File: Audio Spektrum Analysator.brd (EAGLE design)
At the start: 144.8 x 98.7 mm, 157 parts, among them IC1 LM324N, IC10 LM3914N, IC11 LM3914N, IC12 LM3914N, IC13 LM3914N, IC2 LM324N, IC3 LM324N, IC4 LM3914N, IC5 LM3914N, IC6 LM3914N, IC7 LM3914N, IC8 LM3914N, IC9 LM3914N, J2 DCJ0202, M1 ELECTRET_MICROPHON-F6050AP

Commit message: moved names, added testpoints
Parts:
- added TP4, TP5: TPPAD1-20, testpad:P1-20
- moved TP3 46.9 mm to (108.0, 12.7)
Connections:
- net RHI: now also TP4.TP
- net RLO: now also TP5.TP
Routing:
- net RLO: track 149.6 -> 171.8 mm, vias 9 -> 11
- net RHI: track 163.9 -> 183.0 mm, vias 0 -> 1
- net VER: track 176.2 -> 172.2 mm

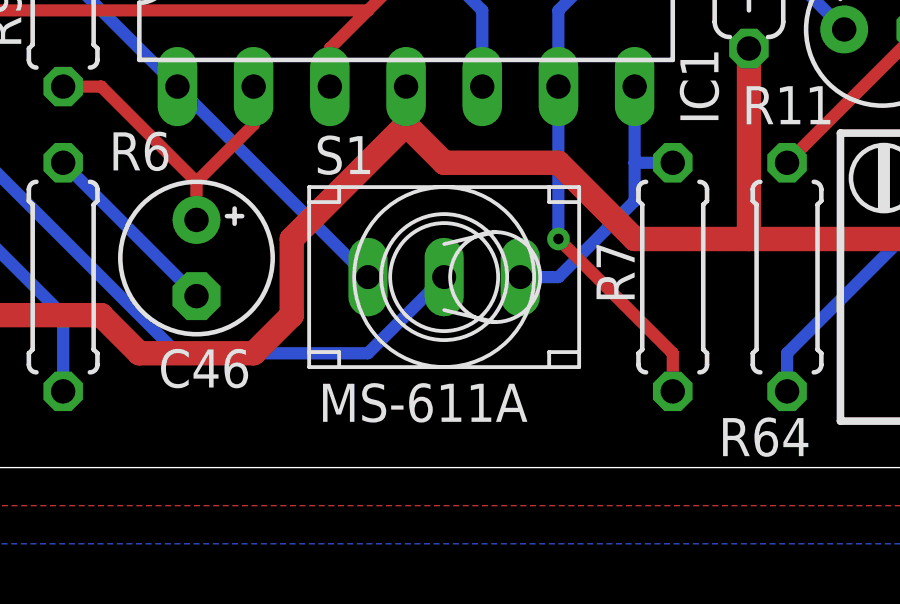
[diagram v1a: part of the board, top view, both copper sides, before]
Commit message: replaced s1
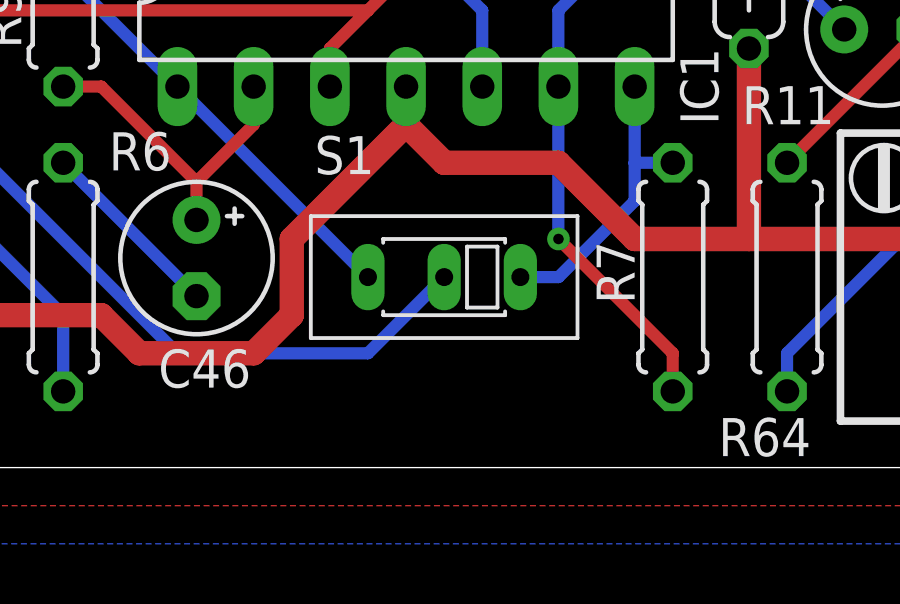
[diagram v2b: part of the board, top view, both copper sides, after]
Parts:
- S1: value MS-611A -> SPDT; device 1_Robo-Lib:MS-611A -> Jakobs_LBR:SPDT
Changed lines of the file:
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@@
 <layer number="44" name="Drills" color="7" fill="1" visible="yes" active="yes"/>
 <layer number="45" name="Holes" color="7" fill="1" visible="yes" active="yes"/>
-<layer number="46" name="Milling" color="3" fill="1" visible="no" active="yes"/>
+<layer number="46" name="Milling" color="3" fill="1" visible="yes" active="yes"/>
 <layer number="47" name="Measures" color="7" fill="1" visible="no" active="yes"/>
 <layer number="48" name="Document" color="7" fill="1" visible="no" active="yes"/>
@@
 <attribute name="VALUE" x="43.2562" y="68.326" size="1.27" layer="27" font="vector" ratio="10" rot="R270"/>
 </element>
-<element name="S1" library="1_Robo-Lib" package="MS-611A" value="MS-611A" x="46.99" y="6.35" smashed="yes">
-<attribute name="LENGTH" value="9mm" x="46.99" y="6.35" size="1.778" layer="27" display="off"/>
+<element name="S1" library="Jakobs_LBR" package="SPDT" value="SPDT" x="46.99" y="6.35" smashed="yes">
 <attribute name="NAME" x="42.672" y="9.779" size="1.27" layer="25" font="vector" ratio="10"/>
-<attribute name="PINPITCH" value="2.54mm" x="46.99" y="6.35" size="1.778" layer="27" display="off"/>
-<attribute name="VALUE" x="42.799" y="1.524" size="1.27" layer="25" font="vector" ratio="10"/>
-<attribute name="WIDTH" value="6mm" x="46.99" y="6.35" size="1.778" layer="27" display="off"/>
+<attribute name="VALUE" x="42.799" y="1.524" size="1.27" layer="27" font="vector" ratio="10"/>
 </element>
 <element name="TP3" library="testpad" library_urn="urn:adsk.eagle:library:385" package="P1-20" package3d_urn="urn:adsk.eagle:package:27950/1" value="TPPAD1-20" x="107.95" y="12.7" smashed="yes">

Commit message: Ich habe fertig V1.0
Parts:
- removed M1: ELECTRET_MICROPHON-F6050AP, microphon:F6050AP
- removed R70: 1k, resistor:0207/7
- added Q1: (no value), adafruit:9.7ELECTRET
- added R62: 1k2, resistor:0207/7
- C10: value 1u -> 22n; device resistor:E2,5-5 -> resistor:C025-024X044
- C11: value 1u -> 10n; device resistor:E2,5-5 -> resistor:C025-024X044
- C12: value 4n7 -> 1u; device resistor:C025-024X044 -> resistor:E2,5-5
- C13: value 2n2 -> 1u; device resistor:C025-024X044 -> resistor:E2,5-5
- C14, C18: value 1n2 -> 4n7
- C15, C19: value 620p -> 2n2
- C16: value 4n7 -> 1n2
- C17: value 2n2 -> 620p
- C2, C4: value 100n -> 2u2; device resistor:C050-024X044 -> resistor:E2,5-5
- C20: value 1u -> 1n2; device resistor:E2,5-5 -> resistor:C025-024X044
- C21: value 1u -> 620p; device resistor:E2,5-5 -> resistor:C025-024X044
- C24: value 330p -> 1u; device resistor:C025-024X044 -> resistor:E2,5-5
- C25: value 160p -> 1u; device resistor:C025-024X044 -> resistor:E2,5-5
- C26, C30: value 82p -> 330p
- C27, C31: value 39p -> 160p
- C28: value 330p -> 82p
- C29: value 160p -> 39p
- C32: value 1u -> 82p; device resistor:E2,5-5 -> resistor:C025-024X044
- C33: value 1u -> 39p; device resistor:E2,5-5 -> resistor:C025-024X044
- C36, C37: value 100n -> 1u; device resistor:C050-024X044 -> resistor:E2,5-5
- C46, C47: value 2u2 -> 100n; device resistor:E2,5-5 -> resistor:C050-024X044
- C6: value 22n -> 100n; device resistor:C025-024X044 -> resistor:C050-024X044
- C7: value 10n -> 100n; device resistor:C025-024X044 -> resistor:C050-024X044
- J1: device Jakobs_LBR:2.5MM-AUX_PC -> Jakobs_LBR:2,5MM-AUX_JACK
- R11: value 50k -> 1k; device resistor:RTRIM64W -> rcl:0207/7
- R12, R22, R23, R36, R37, R38: value 120k -> 100k; device resistor:0207/7 -> rcl:0207/7
- R13: value 120k -> 10k
- R14: value 120k -> 1M; device resistor:0207/7 -> rcl:0207/7
- R16: value 22k -> 120k
- R17, R18, R27, R28, R29, R30, R40, R41, R42: value 1M -> 120k
- R19: value 120k -> 22k
- R20, R21, R32, R33, R34, R35: value 120k -> 1M
- R39: value 1M -> 100k; device resistor:0207/7 -> rcl:0207/7
- R4: value 47k -> 10k; device rcl:0207/7 -> resistor:RTRIM64W
- R43, R44: value 20k -> 120k
- R45: value 100k -> 120k; device rcl:0207/7 -> resistor:0207/7
- R46, R47: value 1k2 -> 120k
- R48, R50: value 100k -> 1M; device rcl:0207/7 -> resistor:0207/7
- R49, R51: value 1k2 -> 1M
- R5: value 47k -> 50k; device rcl:0207/7 -> resistor:RTRIM64W
- R53, R55: value 1k2 -> 100k; device resistor:0207/7 -> rcl:0207/7
- R56: value 100k -> 9k; device rcl:0207/7 -> resistor:0207/7
- R57: value 1k2 -> 1k
- R58: value 100k -> 20k; device rcl:0207/7 -> resistor:0207/7
- R59: value 1k2 -> 20k
- R6: value 10k -> 47k
- R60, R66, R67: value 100k -> 1k2; device rcl:0207/7 -> resistor:0207/7
- R63: value 47k -> 1k2; device rcl:0207/7 -> resistor:0207/7
- R64: value 1k -> 1k2; device rcl:0207/7 -> resistor:0207/7
- R65: value 1M -> 1k2; device rcl:0207/7 -> resistor:0207/7
- R69: value 9k -> 1k2
- R7: value 10k -> 47k; device resistor:0207/7 -> rcl:0207/7
- R8: device resistor:RTRIM64W -> rcl:0207/7
- R9: value 100k -> 47k
- moved R69 140.7 mm to (141.6, 59.7)
- moved R60 126.4 mm to (15.9, 59.7), turned to 270 degrees
- moved C36 118.1 mm to (127.0, 38.1)
- moved C37 118.1 mm to (141.0, 38.1)
- moved R44 114.5 mm to (121.9, 6.35), turned to 270 degrees
- moved R59 112.2 mm to (15.9, 49.5), turned to 90 degrees
- moved R58 112.0 mm to (15.9, 39.4), turned to 270 degrees
- moved R57 112.0 mm to (1.91, 52.8)
- moved R56 111.8 mm to (1.91, 43.2), turned to 270 degrees
- moved R68 111.8 mm to (127.6, 59.7)
- moved R61 111.8 mm to (29.8, 59.7)
- moved R46 102.6 mm to (127.0, 26.7), turned to 90 degrees
- moved R66 92.7 mm to (99.7, 59.7), turned to 270 degrees
- moved R36 92.6 mm to (43.8, 47.0), turned to 90 degrees
- moved R45 92.6 mm to (127.0, 6.35), turned to 270 degrees
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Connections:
- net GND: now also C12.-, C13.-, C24.-, C25.-, C36.-, C37.-, C46.2, C47.2, C6.2, C7.2, J1.4, J2.2, Q1.-, R17.1, R18.1, R22.1, R28.1, R29.1, R30.1, R31.1, R39.1, R4.2, R5.2, R62.1, R63.1, R64.1, R69.1, R7.1; no longer C10.-, C11.-, C2.2, C20.-, C21.-, C32.-, C33.-, C36.2, C37.2, C4.2, M1.1, R11.2, R15.1, R24.1, R25.1, R26.1, R35.1, R48.1, R49.1, R5.1, R50.1, R51.1, R56.1, R58.1, R70.1, R8.2
- net N$1: now also J1.2; no longer J1.4
- net N$10: now also R13.2; no longer R7.2
- net N$108: now also R60.2; no longer R68.2
- net N$12: now also C4.+; no longer C3.+
- net N$125: now also C18.2, R32.2; no longer C16.2, R27.2
- net N$13: now also Q1.+; no longer M1.2
- net N$130: now also C14.2, R32.1; no longer C12.2, R27.1
- net N$133: now also C10.2, R20.2; no longer C8.2, R17.2
- net N$134: now also C8.2, R20.1; no longer C6.2, R17.1
- net N$135: now also C21.2, R35.2; no longer C19.2, R30.2
- net N$136: now also C10.1, R15.2, R17.2; no longer C6.1, R12.2, R14.2
- net N$138: now also C11.2, R21.2; no longer C9.2, R18.2
- net N$139: now also C9.2, R21.1; no longer C7.2, R18.1
- net N$140: now also C14.1, C18.1, R24.2, R28.2; no longer C12.1, C16.1, R19.2, R23.2
- net N$141: now also C11.1, R16.2, R18.2; no longer C7.1, R13.2, R15.2
- net N$144: now also C19.2, R33.2; no longer C17.2, R28.2
- net N$145: now also C15.2, R33.1; no longer C13.2, R28.1
- net N$146: now also C17.2, R35.1; no longer C15.2, R30.1
- net N$147: now also C15.1, C19.1, R25.2, R29.2; no longer C13.1, C17.1, R20.2, R24.2
- net N$149: now also C20.2, R34.2; no longer C18.2, R29.2
- net N$150: now also C16.2, R34.1; no longer C14.2, R29.1
- net N$151: now also C30.2, R48.2; no longer C28.2, R39.2
- net N$152: now also C16.1, C20.1, R26.2, R30.2; no longer C14.1, C18.1, R21.2, R25.2
- net N$154: now also C17.1, C21.1, R27.2, R31.2; no longer C15.1, C19.1, R22.2, R26.2
- net N$156: now also C26.2, R48.1; no longer C24.2, R39.1
- net N$157: now also C26.1, C30.1, R40.2, R44.2; no longer C24.1, C28.1, R31.2, R35.2
- net N$159: now also C31.2, R49.2; no longer C29.2, R40.2
- net N$160: now also C27.2, R49.1; no longer C25.2, R40.1
- net N$161: now also C27.1, C31.1, R41.2, R45.2; no longer C25.1, C29.1, R32.2, R36.2
- net N$163: now also C32.2, R50.2; no longer C30.2, R41.2
- net N$164: now also C28.2, R50.1; no longer C26.2, R41.1
- net N$165: now also C28.1, C32.1, R42.2, R46.2; no longer C26.1, C30.1, R33.2, R37.2
- net N$167: now also C33.2, R51.2; no longer C31.2, R42.2
- net N$168: now also C29.2, R51.1; no longer C27.2, R42.1
- net N$169: now also C29.1, C33.1, R43.2, R47.2; no longer C27.1, C31.1, R34.2, R38.2
- net N$2: now also J1.3; no longer J1.2
- net N$29: now also R62.2; no longer R47.2
- net N$3: now also R9.1; no longer R63.1
- net N$30: now also R61.2; no longer R46.2
- net N$31: now also C2.-, R8.2; no longer C46.-, R6.2
- net N$4: now also R6.1, R7.2; no longer R4.1, R5.2
- net N$42: now also R63.2; no longer R49.2
- net N$43: now also R64.2; no longer R51.2
- net N$44: now also R4.3, R8.1; no longer R6.1, R8.3
- net N$5: now also C2.+, R12.1; no longer C46.+, R9.1
- net N$55: now also R66.2; no longer R55.2
- net N$56: now also R65.2; no longer R53.2
- net N$57: now also C3.+, R13.1; no longer C47.+, R7.1
- net N$6: now also R12.2; no longer R9.2
- net N$68: now also R67.2; no longer R57.2
- net N$69: now also R68.2; no longer R59.2
- net N$70: now also C3.-, R11.2; no longer C47.-, R64.2
- net N$81: now also R69.2; no longer R61.2
- net N$83: now also R11.1, R5.3; no longer R11.3, R64.1
- net OUT1: now also C12.+, R22.2; no longer C10.+, R66.2
- net OUT10: now also C37.+, R55.2; no longer C35.+, R60.2
- net OUT2: now also C13.+, R23.2; no longer C11.+, R67.2
- net OUT3: now also C22.+, R36.2; no longer C20.+, R45.2
- net OUT4: now also C23.+, R37.2; no longer C21.+, R48.2
- net OUT5: now also C24.+, R38.2; no longer C22.+, R50.2
- net OUT6: now also C25.+, R39.2; no longer C23.+, R52.2
- net OUT7: now also C34.+, R52.2; no longer C32.+, R54.2
- net OUT8: now also C35.+, R53.2; no longer C33.+, R56.2
- net OUT9: now also C36.+, R54.2; no longer C34.+, R58.2
- net REF: now also R19.1; no longer R16.1
- net RHI: now also R58.1, R59.2; no longer R43.1, R44.2
- net RLO: now also R56.1, R57.2; no longer R69.1, R70.2
- net V+: now also C46.1, C47.1, C6.1, C7.1, R19.2, R56.2, R58.2, R6.2, R9.2; no longer C2.1, C36.1, C37.1, C4.1, R16.2, R4.2, R43.2, R63.2, R69.2
- net VER: now also C4.-, R14.2, R15.1, R16.1, R24.1, R25.1, R26.1, R27.1, R40.1, R41.1, R42.1, R43.1; no longer C3.-, R12.1, R13.1, R19.1, R20.1, R21.1, R22.1, R31.1, R32.1, R33.1, R34.1, R65.2
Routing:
- net N$1: track 7.51 -> 15.7 mm
- net N$13: track 12.5 -> 15.4 mm
- net N$2: track 21.8 -> 20.0 mm
- net N$4: track 60.3 -> 61.8 mm
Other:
- board text added: "GND"
- board text added: "RHI"
- board text added: "RLO"
- board text added: "V+"
- board text added: "VER"
